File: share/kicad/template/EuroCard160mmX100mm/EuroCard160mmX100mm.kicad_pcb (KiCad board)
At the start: 2 copper layers, 159.8 x 99.8 mm, 0 parts

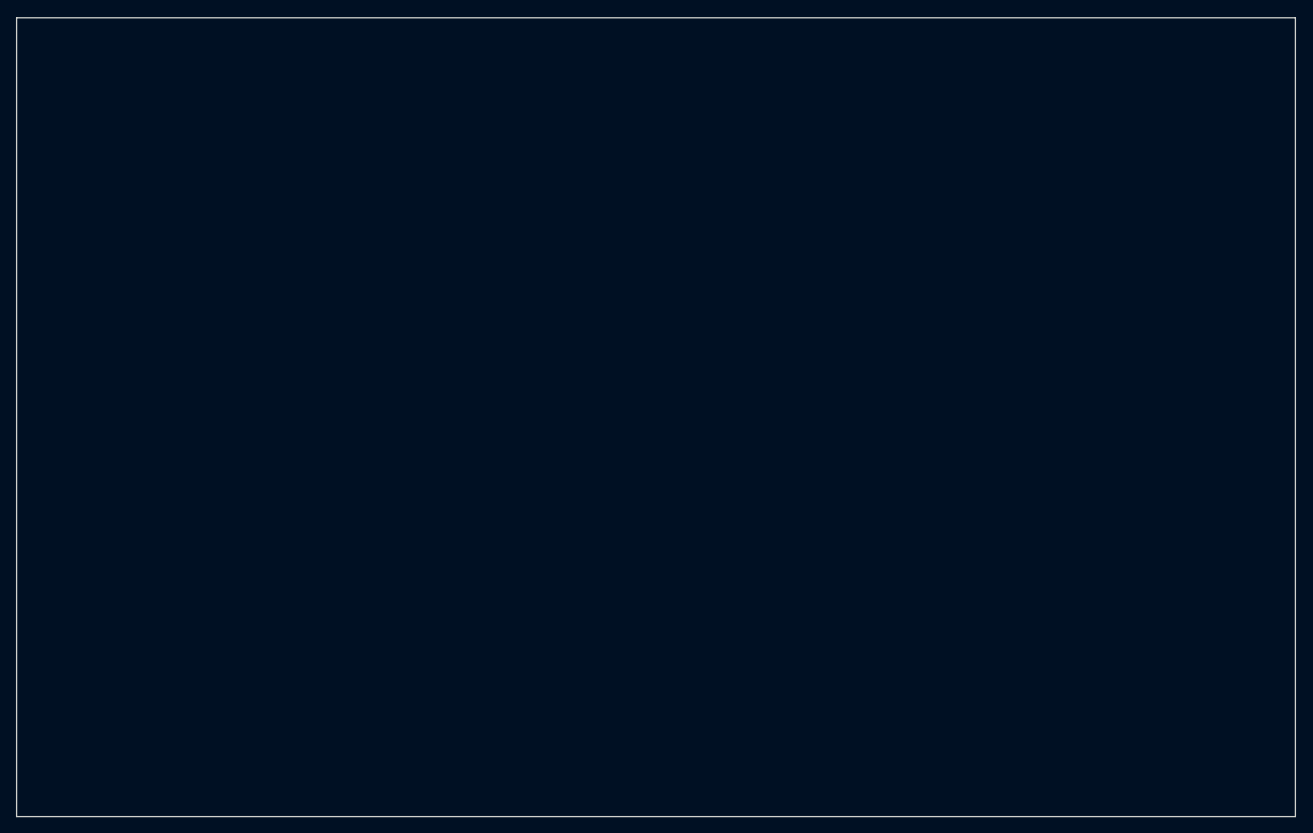
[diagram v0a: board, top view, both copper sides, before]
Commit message: Remove KiCad V4.0.7
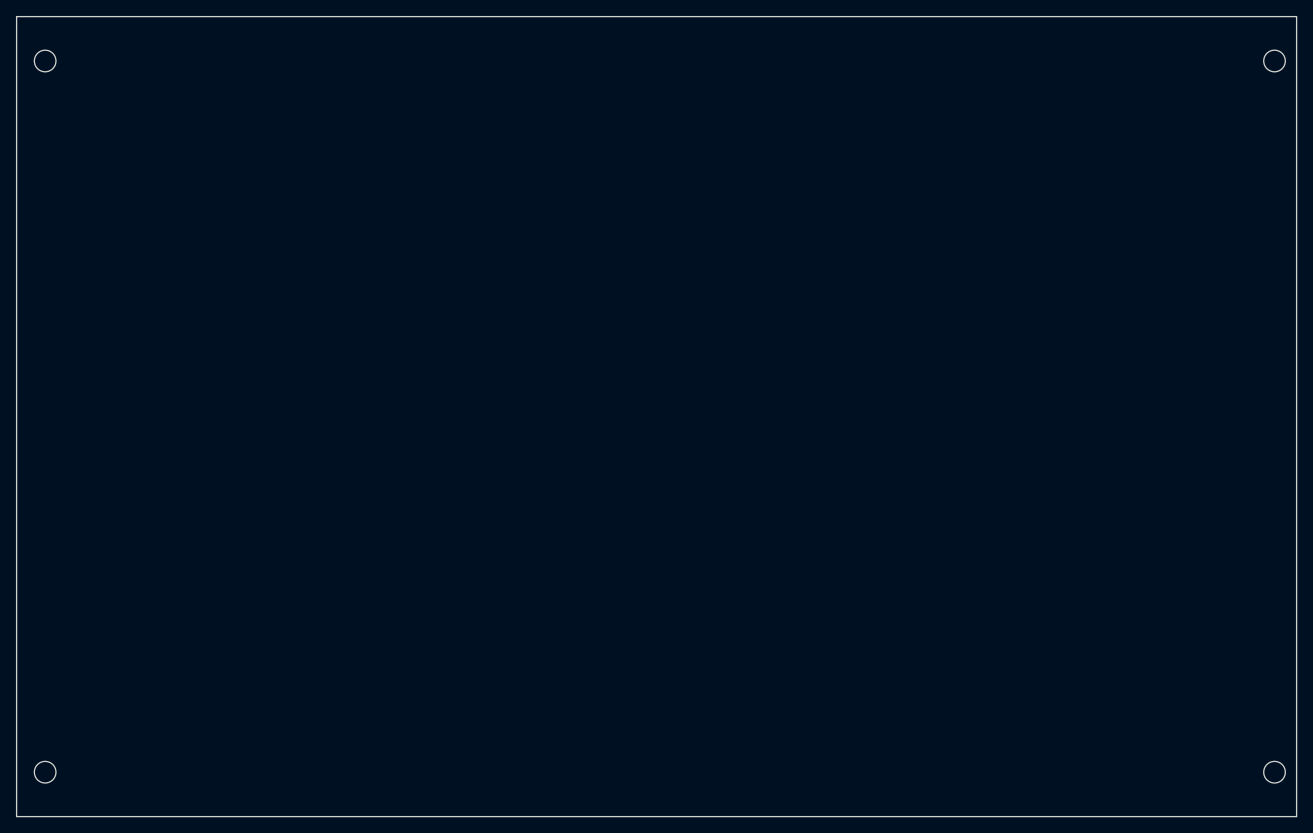
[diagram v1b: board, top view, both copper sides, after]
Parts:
- added MH1: MountingHole_2.7mm_M2.5_DIN965, MountingHole:MountingHole_2.7mm_M2.5_DIN965, F.Cu at (58.6, 50.5)
- added MH2: MountingHole_2.7mm_M2.5_DIN965, MountingHole:MountingHole_2.7mm_M2.5_DIN965, F.Cu at (58.6, 139.4)
- added MH3: MountingHole_2.7mm_M2.5_DIN965, MountingHole:MountingHole_2.7mm_M2.5_DIN965, F.Cu at (212.2, 50.5)
- added MH4: MountingHole_2.7mm_M2.5_DIN965, MountingHole:MountingHole_2.7mm_M2.5_DIN965, F.Cu at (212.2, 139.4)
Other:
- board size 159.8 x 99.8 mm -> 160 x 100 mm
- net class Default removed
- rule pad_to_mask_clearance: 0.2 -> 0
- board text added: "Mounting holes are optional Keepout areas are for for guide rails"
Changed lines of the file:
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@@
-(kicad_pcb (version 20170123) (host pcbnew "(2017-07-16 revision e797af331)-master")
+(kicad_pcb (version 20211014) (generator pcbnew)
   (general
     (thickness 1.6)
-    (drawings 4)
-    (tracks 0)
-    (zones 0)
-    (modules 0)
-    (nets 1)
   )
-  (page A4)
+  (paper "A4")
   (layers
-    (0 F.Cu signal)
-    (31 B.Cu signal)
-    (32 B.Adhes user)
-    (33 F.Adhes user)
-    (34 B.Paste user)
-    (35 F.Paste user)
-    (36 B.SilkS user)
-    (37 F.SilkS user)
-    (38 B.Mask user)
-    (39 F.Mask user)
-    (40 Dwgs.User user)
-    (41 Cmts.User user)
-    (42 Eco1.User user)
-    (43 Eco2.User user)
-    (44 Edge.Cuts user)
-    (45 Margin user)
-    (46 B.CrtYd user)
-    (47 F.CrtYd user)
-    (48 B.Fab user)
-    (49 F.Fab user)
+    (0 "F.Cu" signal)
+    (31 "B.Cu" signal)
+    (32 "B.Adhes" user "B.Adhesive")
+    (33 "F.Adhes" user "F.Adhesive")
+    (34 "B.Paste" user)
+    (35 "F.Paste" user)
+    (36 "B.SilkS" user "B.Silkscreen")
+    (37 "F.SilkS" user "F.Silkscreen")
+    (38 "B.Mask" user)
+    (39 "F.Mask" user)
+    (40 "Dwgs.User" user "User.Drawings")
+    (41 "Cmts.User" user "User.Comments")
+    (42 "Eco1.User" user "User.Eco1")
+    (43 "Eco2.User" user "User.Eco2")
+    (44 "Edge.Cuts" user)
+    (45 "Margin" user)
+    (46 "B.CrtYd" user "B.Courtyard")
+    (47 "F.CrtYd" user "F.Courtyard")
+    (48 "B.Fab" user)
+    (49 "F.Fab" user)
   )
   (setup
-    (last_trace_width 0.25)
-    (trace_clearance 0.2)
-    (zone_clearance 0.508)
-    (zone_45_only no)
-    (trace_min 0.2)
-    (segment_width 0.2)
-    (edge_width 0.15)
-    (via_size 0.8)
-    (via_drill 0.4)
-    (via_min_size 0.4)
-    (via_min_drill 0.3)
-    (uvia_size 0.3)
-    (uvia_drill 0.1)
-    (uvias_allowed no)
-    (uvia_min_size 0.2)
-    (uvia_min_drill 0.1)
-    (pcb_text_width 0.3)
-    (pcb_text_size 1.5 1.5)
-    (mod_edge_width 0.15)
-    (mod_text_size 1 1)
-    (mod_text_width 0.15)
-    (pad_size 1.524 1.524)
-    (pad_drill 0.762)
-    (pad_to_mask_clearance 0.2)
-    (aux_axis_origin 0 0)
+    (stackup
+      (layer "F.SilkS" (type "Top Silk Screen"))
+      (layer "F.Paste" (type "Top Solder Paste"))
+      (layer "F.Mask" (type "Top Solder Mask") (color "Green") (thickness 0.01))
+      (layer "F.Cu" (type "copper") (thickness 0.035))
+      (layer "dielectric 1" (type "core") (thickness 1.51) (material "FR4") (epsilon_r 4.5) (loss_tangent 0.02))
+      (layer "B.Cu" (type "copper") (thickness 0.035))
+      (layer "B.Mask" (type "Bottom Solder Mask") (color "Green") (thickness 0.01))
+      (layer "B.Paste" (type "Bottom Solder Paste"))
+      (layer "B.SilkS" (type "Bottom Silk Screen"))
+      (copper_finish "None")
+      (dielectric_constraints no)
+    )
+    (pad_to_mask_clearance 0)
+    (aux_axis_origin 55 145)
     (grid_origin 55 145)
-    (visible_elements FFFFFF7F)
     (pcbplotparams
-      (layerselection 0x00030_ffffffff)
+      (layerselection 0x0000030_ffffffff)
+      (disableapertmacros false)
       (usegerberextensions false)
+      (usegerberattributes true)
+      (usegerberadvancedattributes true)
+      (creategerberjobfile true)
+      (svguseinch false)
+      (svgprecision 6)
       (excludeedgelayer true)
-      (linewidth 0.100000)
       (plotframeref false)
       (viasonmask false)
@@
       (hpglpennumber 1)
       (hpglpenspeed 20)
-      (hpglpendiameter 15)
+      (hpglpendiameter 15.000000)
+      (dxfpolygonmode true)
+      (dxfimperialunits true)
+      (dxfusepcbnewfont true)
       (psnegative false)
       (psa4output false)
@@
       (plotvalue true)
       (plotinvisibletext false)
-      (padsonsilk false)
+      (sketchpadsonfab false)
       (subtractmaskfromsilk false)
       (outputformat 1)
@@
       (drillshape 0)
       (scaleselection 1)
-      (outputdirectory ""))
+      (outputdirectory "")
+    )
   )
   (net 0 "")
-  (net_class Default "This is the default net class."
-    (clearance 0.2)
-    (trace_width 0.25)
-    (via_dia 0.8)
-    (via_drill 0.4)
-    (uvia_dia 0.3)
-    (uvia_drill 0.1)
+  (footprint "MountingHole:MountingHole_2.7mm_M2.5_DIN965" locked (layer "F.Cu")
+    (at 212.24 139.45)
+    (descr "Mounting Hole 2.7mm, no annular, M2.5, DIN965")
+    (tags "mounting hole 2.7mm no annular m2.5 din965")
+    (attr exclude_from_pos_files exclude_from_bom)
+    (fp_text reference "MH4" (at 0 -3.35) (layer "F.SilkS") hide
+      (effects (font (size 1 1) (thickness 0.15)))
+    )
+    (fp_text value "MountingHole_2.7mm_M2.5_DIN965" (at 0 3.35) (layer "F.Fab") hide
+      (effects (font (size 1 1) (thickness 0.15)))
+    )
+    (fp_text user "${REFERENCE}" (at 0.3 0) (layer "F.Fab") hide
+      (effects (font (size 1 1) (thickness 0.15)))
+    )
+    (fp_circle (center 0 0) (end 2.35 0) (layer "Cmts.User") (width 0.15) (fill none))
+    (fp_circle (center 0 0) (end 2.6 0) (layer "F.CrtYd") (width 0.05) (fill none))
+    (pad "" np_thru_hole circle locked (at 0 0) (size 2.7 2.7) (drill 2.7) (layers *.Cu *.Mask))
   )
-  (gr_line (start 55 145) (end 214.85 145) (angle 90) (layer Edge.Cuts) (width 0.15))
-  (gr_line (start 55 45.15) (end 55 145) (angle 90) (layer Edge.Cuts) (width 0.15))
-  (gr_line (start 214.84 45.15) (end 55 45.15) (angle 90) (layer Edge.Cuts) (width 0.15))
-  (gr_line (start 214.85 145) (end 214.85 45.15) (angle 90) (layer Edge.Cuts) (width 0.15))
+  (footprint "MountingHole:MountingHole_2.7mm_M2.5_DIN965" (layer "F.Cu")
+    (at 58.57 50.55)
+    (descr "Mounting Hole 2.7mm, no annular, M2.5, DIN965")
+    (tags "mounting hole 2.7mm no annular m2.5 din965")
+    (attr exclude_from_pos_files exclude_from_bom)
+    (fp_text reference "MH1" (at 0 -3.35) (layer "F.SilkS") hide
+      (effects (font (size 1 1) (thickness 0.15)))
+    )
+    (fp_text value "MountingHole_2.7mm_M2.5_DIN965" (at 0 3.35) (layer "F.Fab") hide
+      (effects (font (size 1 1) (thickness 0.15)))
+    )
+    (fp_text user "${REFERENCE}" (at 0.3 0) (layer "F.Fab") hide
+      (effects (font (size 1 1) (thickness 0.15)))
+    )
+    (fp_circle (center 0 0) (end 2.35 0) (layer "Cmts.User") (width 0.15) (fill none))
+    (fp_circle (center 0 0) (end 2.6 0) (layer "F.CrtYd") (width 0.05) (fill none))
+    (pad "" np_thru_hole circle locked (at 0 0) (size 2.7 2.7) (drill 2.7) (layers *.Cu *.Mask))
+  )
+  (footprint "MountingHole:MountingHole_2.7mm_M2.5_DIN965" locked (layer "F.Cu")
+    (at 58.57 139.45)
+    (descr "Mounting Hole 2.7mm, no annular, M2.5, DIN965")
+    (tags "mounting hole 2.7mm no annular m2.5 din965")
+    (attr exclude_from_pos_files exclude_from_bom)
+    (fp_text reference "MH2" (at 0 -3.35) (layer "F.SilkS") hide
+      (effects (font (size 1 1) (thickness 0.15)))
+    )
+    (fp_text value "MountingHole_2.7mm_M2.5_DIN965" (at 0 3.35) (layer "F.Fab") hide
+      (effects (font (size 1 1) (thickness 0.15)))
+    )
+    (fp_text user "${REFERENCE}" (at 0.3 0) (layer "F.Fab") hide
+      (effects (font (size 1 1) (thickness 0.15)))
+    )
+    (fp_circle (center 0 0) (end 2.35 0) (layer "Cmts.User") (width 0.15) (fill none))
+    (fp_circle (center 0 0) (end 2.6 0) (layer "F.CrtYd") (width 0.05) (fill none))
+    (pad "" np_thru_hole circle locked (at 0 0) (size 2.7 2.7) (drill 2.7) (layers *.Cu *.Mask))
+  )
+  (footprint "MountingHole:MountingHole_2.7mm_M2.5_DIN965" locked (layer "F.Cu")
+    (at 212.24 50.55)
+    (descr "Mounting Hole 2.7mm, no annular, M2.5, DIN965")
+    (tags "mounting hole 2.7mm no annular m2.5 din965")
+    (attr exclude_from_pos_files exclude_from_bom)
+    (fp_text reference "MH3" (at 0 -3.35) (layer "F.SilkS") hide
+      (effects (font (size 1 1) (thickness 0.15)))
+    )
+    (fp_text value "MountingHole_2.7mm_M2.5_DIN965" (at 0 3.35) (layer "F.Fab") hide
+      (effects (font (size 1 1) (thickness 0.15)))
+    )
+    (fp_text user "${REFERENCE}" (at 0.3 0) (layer "F.Fab") hide
+      (effects (font (size 1 1) (thickness 0.15)))
+    )
+    (fp_circle (center 0 0) (end 2.35 0) (layer "Cmts.User") (width 0.15) (fill none))
+    (fp_circle (center 0 0) (end 2.6 0) (layer "F.CrtYd") (width 0.05) (fill none))
+    (pad "" np_thru_hole circle locked (at 0 0) (size 2.7 2.7) (drill 2.7) (layers *.Cu *.Mask))
+  )
+  (gr_rect locked (start 55 145) (end 215 45) (layer "Edge.Cuts") (width 0.15) (fill none))
+  (gr_text "Mounting holes are optional\nKeepout areas are for for guide rails" (at 55.5 148) (layer "Cmts.User")
+    (effects (font (size 1 1) (thickness 0.15)) (justify left))
+  )
+  (zone (net 0) (net_name "") (layers F&B.Cu) (hatch full 0.508)
+    (connect_pads (clearance 0))
+    (min_thickness 0.254)
+    (keepout (tracks not_allowed) (vias not_allowed) (pads not_allowed ) (copperpour allowed) (footprints not_allowed))
+    (fill (thermal_gap 0.508) (thermal_bridge_width 0.508))
+    (polygon
+      (pts
+        (xy 215 145)
+        (xy 55 145)
+        (xy 55 142.5)
+        (xy 215 142.5)
+      )
+    )
+  )
+  (zone (net 0) (net_name "") (layers F&B.Cu) (hatch full 0.508)
+    (connect_pads (clearance 0))
+    (min_thickness 0.254)
+    (keepout (tracks not_allowed) (vias not_allowed) (pads not_allowed ) (copperpour allowed) (footprints not_allowed))
+    (fill (thermal_gap 0.508) (thermal_bridge_width 0.508))
+    (polygon
+      (pts
+        (xy 215 47.5)
+        (xy 55 47.5)
+        (xy 55 45)
+        (xy 215 45)
+      )
+    )
+  )
 )
